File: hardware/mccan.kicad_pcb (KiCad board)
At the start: 8 copper layers, 200 x 140 mm, 238 parts, among them J1 PWR pigtail -> SS1.5 3w, J2 Prog/UART, J3 FL pigtail -> SS1.0 key A / b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, J4 FR pigtail -> SS1.0 key B / g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, J5 RL pigtail -> SS1.0 key C / b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, J6 RR pigtail -> SS1.0 key D / n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, J7 DENALI pigtail -> SS1.5 3w, J8 CAN pigtail -> SS1.0 2w, Q10 IPT008N06NM5LF, Q11 IPT008N06NM5LF, Q12 MMBT3904, Q2 MMBT3904, Q3 MMBT3904, Q4 NX5020UNBKS, Q5 NX5020UNBKS, Q6 NX5020UNBKS, Q7 NX5020UNBKS, Q8 NX5020UNBKS, Q9 NX5020UNBKS, SW1 BOOT, SW2 EN/RESET, U1 LM5164DDA, U10 LTC4380HMS-2, U2 LM5164DDA, U3 LM51571-Q1, U4 DML3017LDC, U5 ESP32-WROOM-32E-N8, U6 TJA1042T/3, U7 PCA9685PW/Q900, U8 ADG706, U9 BTS7008-2EPA

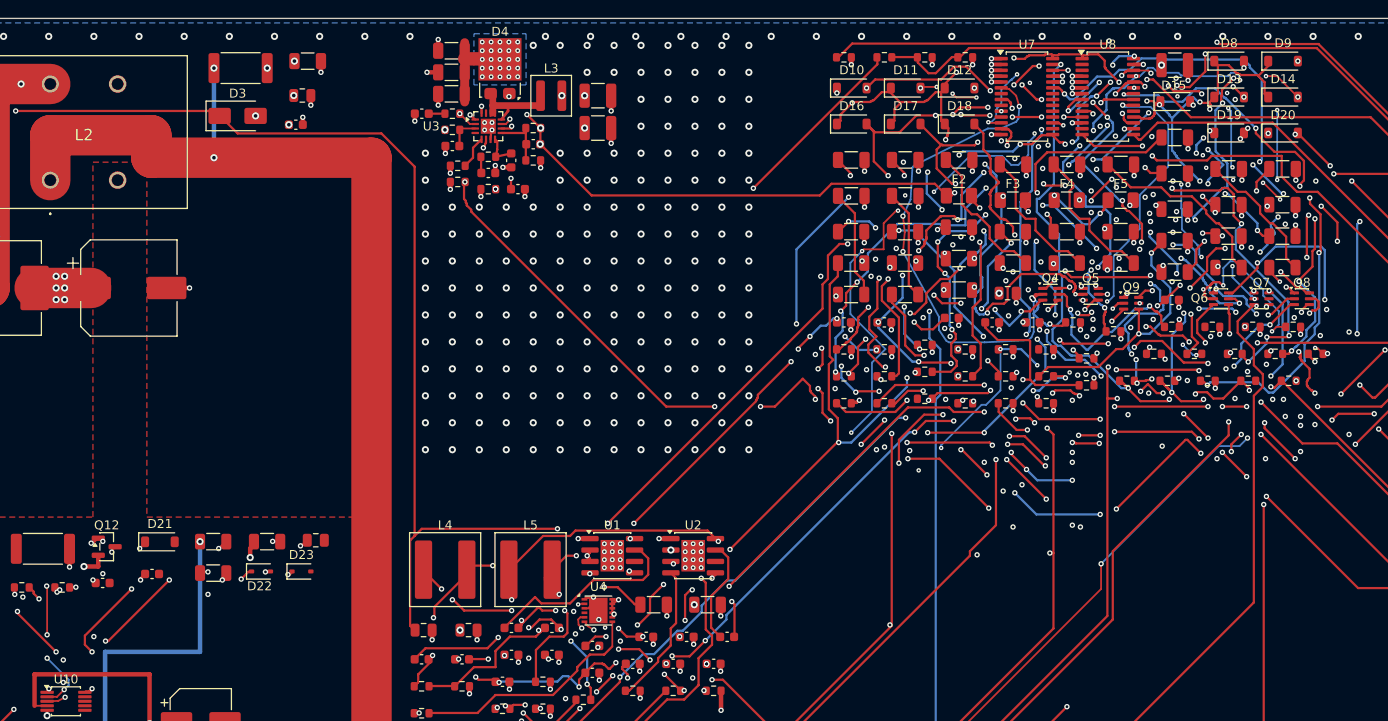
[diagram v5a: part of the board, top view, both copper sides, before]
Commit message: hw(pcb): close PWM_FL_G, PWM_FL_R and PWM_FR_R, and stop hand vias landing on router drills
Three more of U7's PCA9685 outputs routed by hand against the frozen router
copper.  Unconnected pads 13 -> 11; 0 DRC violations, 0 footprint errors.

  /outputs/PWM_FL_G  U7.7 -> R41.1, 9 runs on F.Cu/B.Cu/In2.Cu, 7 vias 0.50/0.20
  /outputs/PWM_FL_R  U7.6 -> R40.1, 6 runs on F.Cu/B.Cu/In2.Cu, 4 vias 0.50/0.20
  /outputs/PWM_FR_R  U7.9 -> R43.1, 8 runs on F.Cu/B.Cu/In5.Cu, 7 vias 0.60/0.30

The committed PWM_FL_R is replaced rather than kept.  U7 pins 6 and 7 are
0.650 mm apart and escape through the same pocket; with the old route in place
pin 7's pocket had 221 reachable cells and no legal via site at all.  Pin 7
first and pin 6 the long way round gets both out.  The two nets meet at
0.202 mm -- the Default class floor exactly, like /EN_BOOST -- so anything
that touches either near U7 pins 6-7 has to re-plan both.

Two ground drops moved, both re-picked by gnd_drops itself; the tally is
unchanged at 139 drop vias for 140 of 141 SMD ground pads, U4.4 still
unserved (a pre-existing missing drop, not a routing failure).

The other half of this is a fab defect, not a routing one.  Six hand vias in
this file sat inside the 0.300 mm hole-to-hole floor against a via the ROUTER
had already placed on the SAME net -- three of the new landings at 0.019,
0.000 and -0.229 mm, and three already committed: Net-(U3-MODE) at 0.025 mm,
Net-(U4-SR) at 0.021 mm and /power_input/U10_GATE at 0.209 mm.  KiCad's DRC
passes every one of them, because it does not test hole-to-hole between two
vias on the same net, and nothing in this repo tested it either.  That would
have shipped as six pairs of 0.30 mm drills microns apart.

All six are fixed the same way: delete our via and end the run ON the
router's, which reaches every layer anyway.  Four of the six were landing on
a router via-in-pad, so the F.Cu stub that followed them went too.
PWM_FL_G's B.Cu run needed one waypoint at (158.700, 52.325) t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
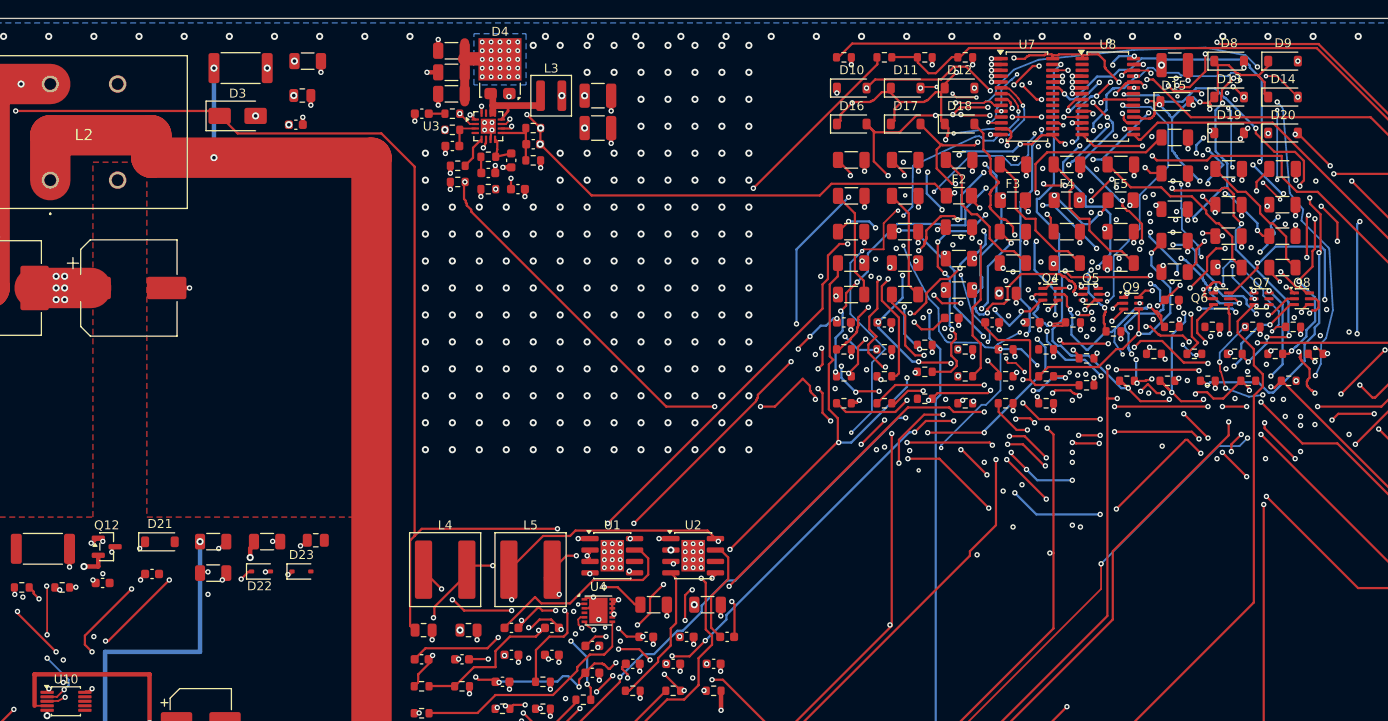
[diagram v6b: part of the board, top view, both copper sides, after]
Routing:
- net /outputs/PWM_FR_R: track 19.4 -> 117.9 mm, vias 4 -> 11
- net /outputs/PWM_FL_G: track 20.2 -> 88.6 mm, vias 2 -> 9
- net /outputs/PWM_FL_R: track 62.0 -> 63.4 mm
- net /power_input/U10_GATE: track 41.5 -> 41.1 mm, vias 6 -> 5
- net Net-(U3-MODE): track 9.95 -> 9.91 mm, vias 3 -> 2
- net Net-(U4-SR): vias 4 -> 3

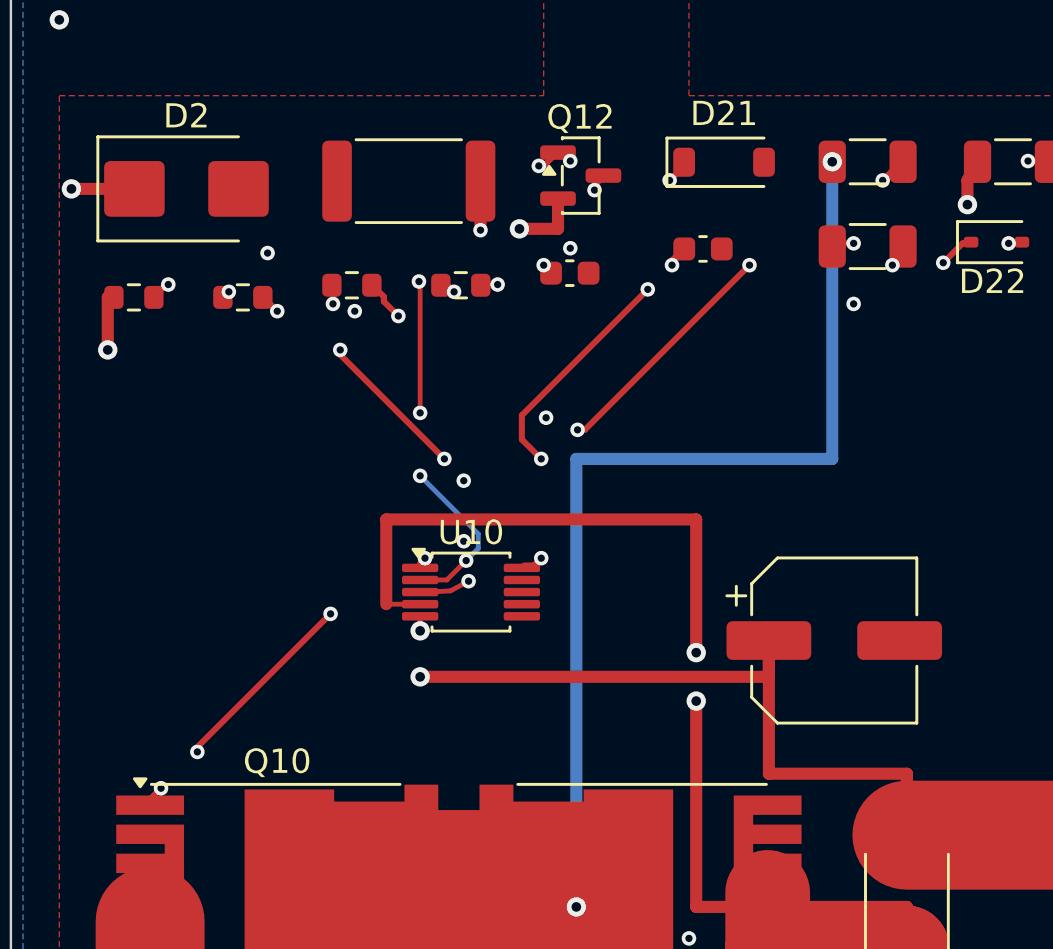
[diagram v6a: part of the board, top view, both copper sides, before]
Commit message: hw(pcb): three router-to-pad junctions etch as hairlines, not connections
With connection_width promoted out of `warning`, KiCad reports three necks on
F.Cu against the board's own 0.2000 mm min_connection:

    0.0589 mm  R101.2 /power_input/U10_DRN  (56.8425, 78.2300)
    0.0790 mm  Q10.1  /power_input/Q10_G    (26.2000, 104.1000)
    0.1346 mm  Q12.1  Net-(Q12-B)           (42.6000, 77.8000)

Same geometry in all three: the router leaves the pad on a 45 degree diagonal at
0.25 mm and crosses the pad outline near its ROUNDED CORNER, so the copper the
track and the pad have in common tapers to a sliver instead of meeting across a
full 0.25 mm.  This is the defect class gen_netclasses.py:88-107 already
described on the retired six-layer board -- "a router via landing off the corner
of Q10 and Q11's gate pads rather than into them ... exactly what this rule is
for and it wants fixing in the routing, not here" -- and Q10_G is that same net.
U10_DRN is the protection FET's drain, Q10_G is Q10's gate, Net-(Q12-B) is the
gate driver's base: a 0.059 mm neck that does not survive the etch tank is an
open gate on the eFuse.

Fixed in the routing, by laying 0.5 mm of hand copper directly over the first leg
of each frozen router run.  Not a re-route: the copper is frozen in
routes_signal.json, the freeze is not regenerated, and FROZEN_DROP would discard
14, 22 and 14 segments to repair a 1 mm junction.  Adding copper on the same net
can only widen the union, so this is the minimal change that fixes the defect
rather than the report of it.  Each segment is collinear with, and no longer
than, the frozen leg it overlays.

0.5 mm is measured.  Full DRC at --severity-all per candidate width:
    0.30 mm  fixes U10_DRN only        (Q10_G 0.0790, Q12-B 0.1100 remain)
    0.35 mm  fixes U10_DRN only        (Q10_G 0.0790, Q12-B 0.0856 remain)
    0.40 mm  fixes U10_DRN and Q10_G   (Q12-B 0.0601 remains -- its pad is only
                                        0.6 mm tall)
    0.50 mm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
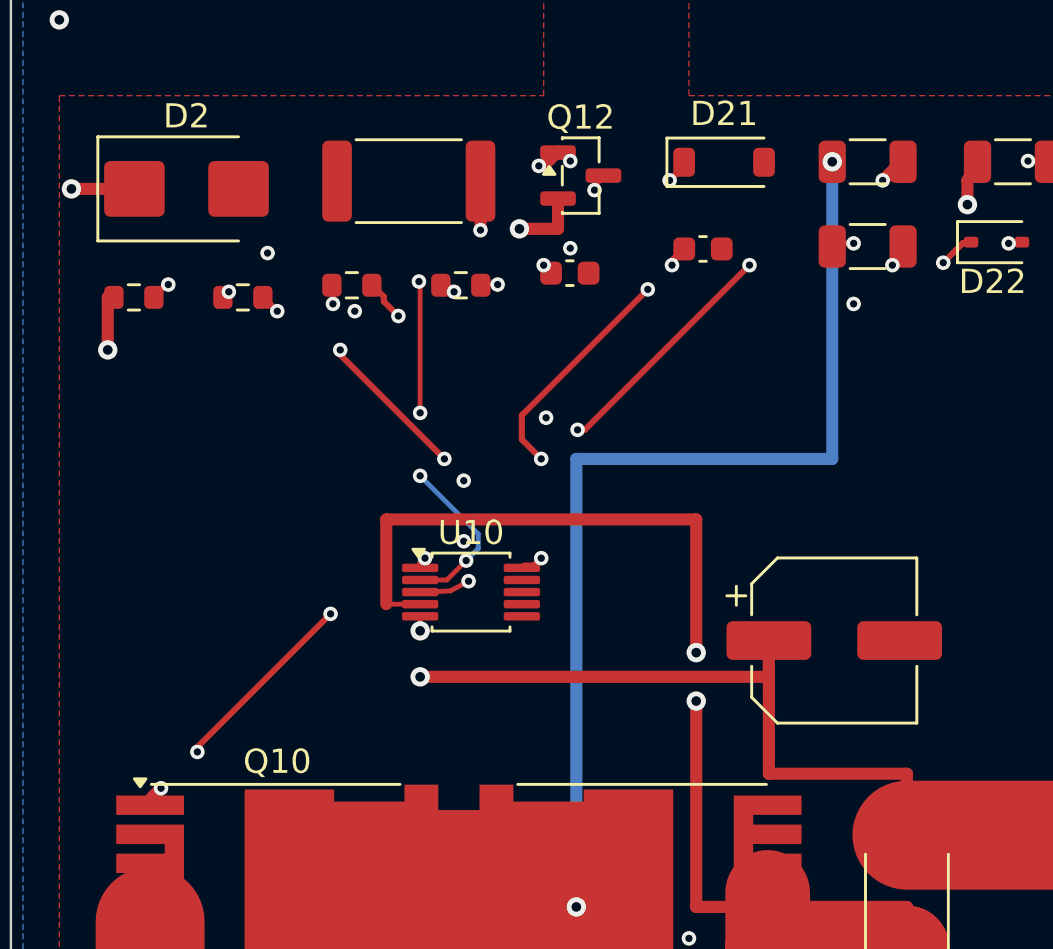
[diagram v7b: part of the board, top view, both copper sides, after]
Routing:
- net /power_input/U10_DRN: track 27.7 -> 28.7 mm
- net Net-(Q12-B): track 37.5 -> 38.3 mm
- net /power_input/Q10_G: track 51.4 -> 52.0 mm
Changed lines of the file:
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@@
 		(net 59)
+	)
+	(segment
+		(start 56.8 78.2)
+		(end 56.1 78.9)
+		(width 0.5)
+		(layer "F.Cu")
+		(net 95)
+	)
+	(segment
+		(start 26.2 104.1)
+		(end 25.8 104.5)
+		(width 0.5)
+		(layer "F.Cu")
+		(net 93)
+	)
+	(segment
+		(start 42.6 77.8)
+		(end 42 78.4)
+		(width 0.5)
+		(layer "F.Cu")
+		(net 131)
 	)
 	(via

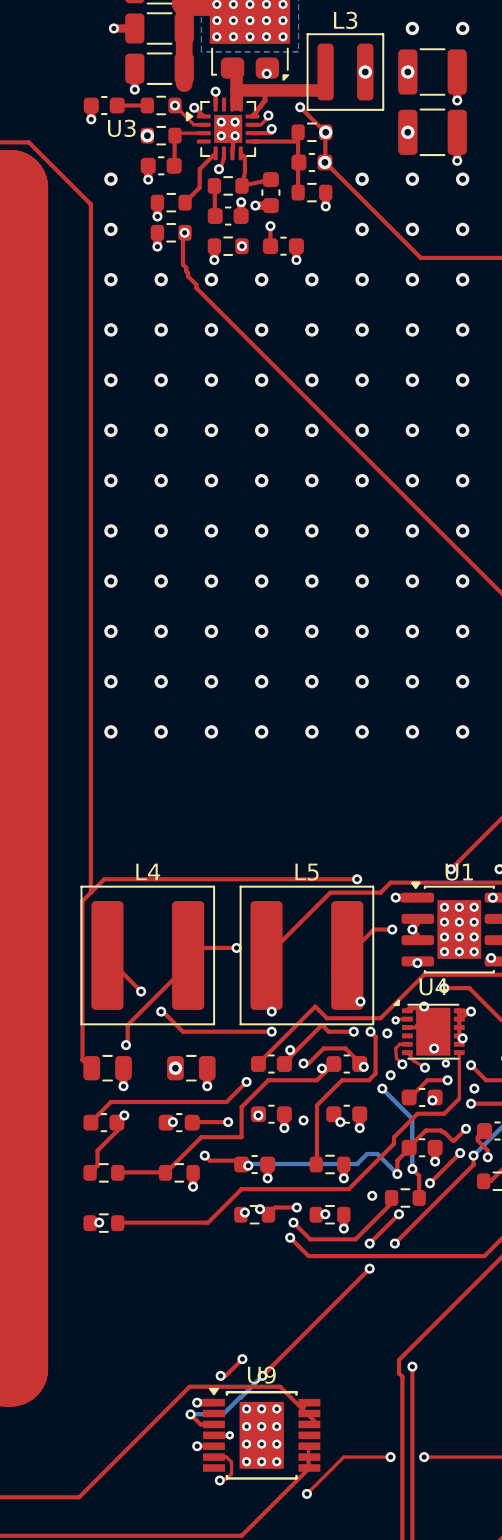
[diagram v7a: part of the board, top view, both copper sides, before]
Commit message: hw(pcb): four dangling vias were copper nothing could ever connect to
Group C of Task 10 fix round 1: what the thirteen [via_dangling] items are, and
which of them are copper rather than a routing gap.  Four were removable; nine
are not, and this says why for each.

Removed, as hand copper (layout_pcb.ROUTE_VIAS):

  ("+24V", 91.825, 32.200) at R12.1 and ("+24V", 91.775, 34.000) at C61.1.
  Their comment said they "drop straight to the +24V pour" so FB_24V's divider
  could read the pour instead of being hauled round on F.Cu.  There is no such
  pour on this board.  /+24V owns one zone -- 24V_D4 on B.Cu, x 84.400..90.200,
  y 21.700..27.400 -- and In4.Cu, which the six-layer stackup would have given
  +24V a piece of, is solid /VBAT since Task 5 reversed the split.  Nearest
  island corner (90.200, 27.400) is 5.07 mm from R12.1 and 6.79 mm from C61.1,
  so both vias landed on bare laminate.  Nothing is lost: the frozen router
  already ties both pads on F.Cu -- (91.800,34.000)-(91.800,32.200) joins them,
  (91.800,32.200)-(90.300,30.700) runs up to the +24V via there.  Neither pad
  is among the 11 unconnected items before or after.

Removed, as frozen router debris (layout_pcb.FROZEN_DROP, previously empty):

  Net-(U3-VCC) -- the whole frozen entry is zero segments and one fanout via at
  (82.825, 30.600) in R15.1.  The net is closed by hand in ROUTES, whose far end
  is that same point, so the drop severs nothing.

  Net-(U9-IS) -- one fanout via at (86.100, 110.000) in U9.4 plus two
  overlapping westward stubs, 0.95 mm and 0.29 mm, both starting on that pad and
  ending in open space.  The net's other pad, R82.1, is 50 mm away and was never
  routed: open with this copper and open without it.  KiCad already reported the
  0.29 mm stub as its own unconnected item.  Measured rather than assumed that
  nothing is foreclosed: `show_pocket.py "Net-(U9-IS)" U9.4` reports the pocket
  UNBOUNDED with 122152 via sites clearing both the copper rule and the 0.30 mm
  hole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
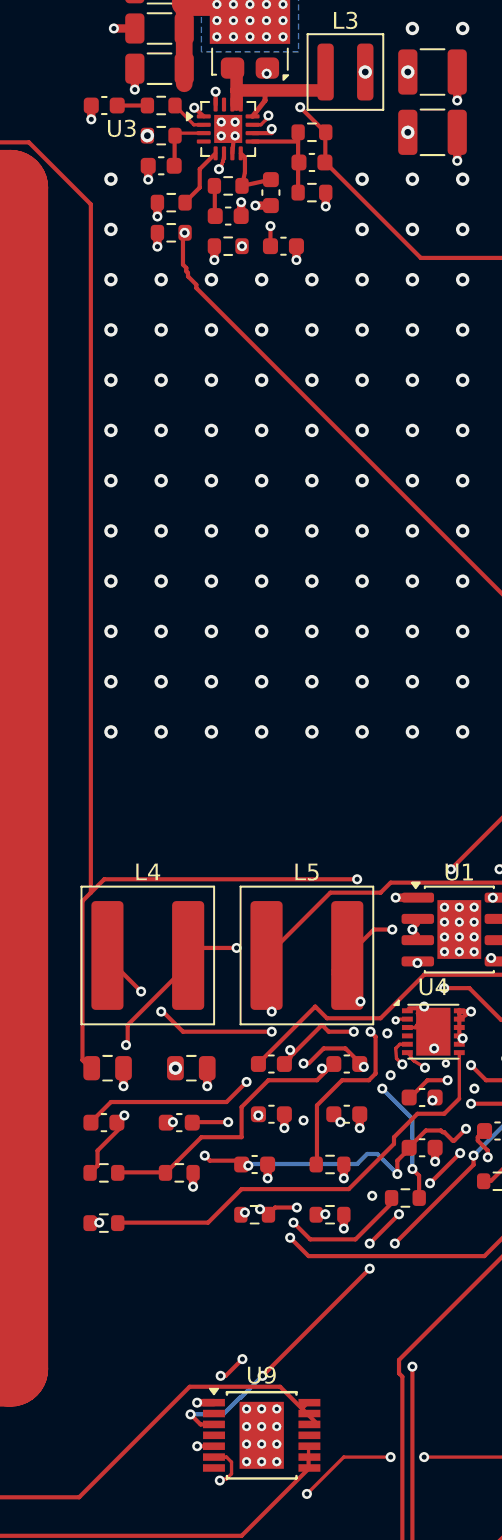
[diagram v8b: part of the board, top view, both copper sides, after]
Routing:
- net Net-(U9-IS): track 1.24 -> 0.00 mm, vias 1 -> 0
- net Net-(U3-VCC): vias 1 -> 0
- net /+24V: vias 34 -> 32
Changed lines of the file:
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@@
 	)
 	(via
-		(at 91.825 32.2)
-		(size 0.8)
-		(drill 0.4)
-		(layers "F.Cu" "B.Cu")
-		(net 4)
-	)
-	(via
-		(at 91.775 34)
-		(size 0.8)
-		(drill 0.4)
-		(layers "F.Cu" "B.Cu")
-		(net 4)
-	)
-	(via
 		(at 88.6 32)
 		(size 0.6)
@@
 		(net 139)
 	)
-	(via
-		(at 82.825 30.6)
-		(size 0.6)
-		(drill 0.3)
-		(layers "F.Cu" "B.Cu")
-		(net 141)
-	)
 	(segment
 		(start 79.4 97.3)
@@
 		(net 151)
 	)
-	(segment
-		(start 86.1 110)
-		(end 85.15 110)
-		(width 0.25)
-		(layer "F.Cu")
-		(net 152)
-	)
-	(segment
-		(start 86.1 110)
-		(end 85.81 110)
-		(width 0.25)
-		(layer "F.Cu")
-		(net 152)
-	)
-	(via
-		(at 86.1 110)
-		(size 0.5)
-		(drill 0.2)
-		(layers "F.Cu" "B.Cu")
-		(net 152)
-	)
 	(zone (net 106) (net_name "GND") (layer "In1.Cu")
